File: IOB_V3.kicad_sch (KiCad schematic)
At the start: 7 parts, among them J1 Conn_01x02, J18 Conn_01x08, J2 Conn_01x03, U1 REF3033

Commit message: Layout WIP
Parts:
- J18: footprint Connector_IDC:IDC-Header_2x04_P2.54mm_Horizontal -> (none)
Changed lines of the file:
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@@
       (effects (font (size 1.27 1.27)) (justify left))
     )
-    (property "Footprint" "Connector_IDC:IDC-Header_2x04_P2.54mm_Horizontal" (id 2) (at 135.255 130.048 0)
+    (property "Footprint" "" (id 2) (at 135.255 130.048 0)
       (effects (font (size 1.27 1.27)) hide)
     )
@@
       (reference "#PWR0134") (unit 1) (value "GNDD") (footprint "")
     )
-    (path "/534d7b1f-d272-47da-b7a1-47aab2c48175/88cdcfe4-f642-4f46-a92c-2fc337766e9b"
+    (path "/534d7b1f-d272-47da-b7a1-47aab2c48175/1e98888a-427d-4a31-a7dd-97b8504ac365"
       (reference "#PWR0135") (unit 1) (value "GNDD") (footprint "")
     )
@@
     )
     (path "/534d7b1f-d272-47da-b7a1-47aab2c48175/5ea038cb-816d-4c36-bb7b-109706ba09b8"
-      (reference "D14") (unit 1) (value "LED") (footprint "LED_THT:LED_D1.8mm_W3.3mm_H2.4mm")
+      (reference "D14") (unit 1) (value "LED") (footprint "LED_SMD:LED_0603_1608Metric")
     )
     (path "/534d7b1f-d272-47da-b7a1-47aab2c48175/3aab0d4c-b03f-4a2b-bb8a-5ed68b4e7455"
-      (reference "D15") (unit 1) (value "LED") (footprint "LED_THT:LED_D1.8mm_W3.3mm_H2.4mm")
+      (reference "D15") (unit 1) (value "LED") (footprint "LED_SMD:LED_0603_1608Metric")
     )
     (path "/534d7b1f-d272-47da-b7a1-47aab2c48175/e259e01a-e686-48b7-b946-0f838b7ef786"
-      (reference "D16") (unit 1) (value "LED") (footprint "LED_THT:LED_D1.8mm_W3.3mm_H2.4mm")
+      (reference "D16") (unit 1) (value "LED") (footprint "LED_SMD:LED_0603_1608Metric")
     )
     (path "/534d7b1f-d272-47da-b7a1-47aab2c48175/08207f2a-291d-44df-8ce7-49d0dd8abd06"
-      (reference "D17") (unit 1) (value "LED") (footprint "LED_THT:LED_D1.8mm_W3.3mm_H2.4mm")
+      (reference "D17") (unit 1) (value "LED") (footprint "LED_SMD:LED_0603_1608Metric")
     )
     (path "/e7136250-cee6-4520-acb7-2950e0829e43/7426b94e-ffc2-452e-843f-c6ffae4705a2/52b8c382-e38e-4898-9fb4-9d3f624b54c7"
@@
     )
     (path "/e7a61089-3c45-4246-9e2f-067953569569"
-      (reference "J18") (unit 1) (value "Conn_01x08") (footprint "Connector_IDC:IDC-Header_2x04_P2.54mm_Horizontal")
+      (reference "J18") (unit 1) (value "Conn_01x08") (footprint "Connector_IDC:IDC-Header_2x04_P2.54mm_Vertical")
     )
     (path "/534d7b1f-d272-47da-b7a1-47aab2c48175/af1dd001-2f93-4b0a-9bcf-1f08059fc4a7"
@@
       (reference "SW2") (unit 1) (value "SW_Push_Dual") (footprint "TXV_Library_Footprints:SW_SPST_CK_RS282G05A3_and_THT")
     )
-    (path "/534d7b1f-d272-47da-b7a1-47aab2c48175/a325f198-534a-4f13-b7fd-b75bb8d3ea8f"
+    (path "/534d7b1f-d272-47da-b7a1-47aab2c48175/179c61ef-4bb1-49e7-a31d-9f9c899ae1c2"
       (reference "SW3") (unit 1) (value "SW_DIP_x08") (footprint "TXV_Library_Footprints:8_Pin_DIP_Switch")
     )

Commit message: Connectors change and part side flip
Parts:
- J18: footprint (none) -> Connector_IDC:IDC-Header_2x04_P2.54mm_Vertical
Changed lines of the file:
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@@
       (effects (font (size 1.27 1.27)) (justify left))
     )
-    (property "Footprint" "" (id 2) (at 135.255 130.048 0)
+    (property "Footprint" "Connector_IDC:IDC-Header_2x04_P2.54mm_Vertical" (id 2) (at 135.255 130.048 0)
       (effects (font (size 1.27 1.27)) hide)
     )
@@
       (reference "#PWR0137") (unit 1) (value "GNDD") (footprint "")
     )
-    (path "/534d7b1f-d272-47da-b7a1-47aab2c48175/86e1fb6b-02f5-44d9-be5a-dcc9d4ffc2e8"
+    (path "/534d7b1f-d272-47da-b7a1-47aab2c48175/31cd537c-8080-4893-996d-cf5dfc73426b"
       (reference "#PWR0138") (unit 1) (value "+5V") (footprint "")
     )
@@
       (reference "#PWR0139") (unit 1) (value "GNDD") (footprint "")
     )
-    (path "/534d7b1f-d272-47da-b7a1-47aab2c48175/573d7cc1-f5ea-48f8-9a0b-1e87d7df0d37"
-      (reference "#PWR0140") (unit 1) (value "GNDD") (footprint "")
+    (path "/534d7b1f-d272-47da-b7a1-47aab2c48175/b6659546-cd20-4177-96e0-bac10a28c326"
+      (reference "#PWR0140") (unit 1) (value "+5V") (footprint "")
     )
     (path "/534d7b1f-d272-47da-b7a1-47aab2c48175/d1457e9e-cd6f-4eac-a387-b31614edcffe"
       (reference "#PWR0141") (unit 1) (value "+3.3V") (footprint "")
     )
-    (path "/534d7b1f-d272-47da-b7a1-47aab2c48175/60eaa4dd-d726-4d7e-a298-4ff4d8f59925"
-      (reference "#PWR0142") (unit 1) (value "+5V") (footprint "")
+    (path "/534d7b1f-d272-47da-b7a1-47aab2c48175/7ebfcebf-b817-46ec-9695-1ccfc3c9960a"
+      (reference "#PWR0142") (unit 1) (value "GNDD") (footprint "")
     )
     (path "/534d7b1f-d272-47da-b7a1-47aab2c48175/221a7428-fe18-4c36-8179-294aaa90dd67"
       (reference "#PWR0143") (unit 1) (value "GNDA") (footprint "")
     )
-    (path "/534d7b1f-d272-47da-b7a1-47aab2c48175/fde89670-540f-4d7e-82e1-0078eae3cc64"
+    (path "/534d7b1f-d272-47da-b7a1-47aab2c48175/2a690fd6-2e13-4f52-bc32-d94631f9979b"
       (reference "#PWR0144") (unit 1) (value "GNDD") (footprint "")
     )
@@
       (reference "J16") (unit 1) (value "Conn_02x04_Odd_Even") (footprint "Connector_PinHeader_1.27mm:PinHeader_2x04_P1.27mm_Vertical_SMD")
     )
-    (path "/534d7b1f-d272-47da-b7a1-47aab2c48175/cd1d0e38-6320-4e6b-bf2a-3f5fcc7479ec"
-      (reference "J17") (unit 1) (value "Conn_01x04_MountingPin") (footprint "Connector_JST:JST_GH_BM04B-GHS-TBT_1x04-1MP_P1.25mm_Vertical")
+    (path "/534d7b1f-d272-47da-b7a1-47aab2c48175/ab44cab5-203b-4fac-b4ee-b824a1ef8e82"
+      (reference "J17") (unit 1) (value "TFC-103-01-F-D") (footprint "SAMTEC_TFC-103-01-F-D")
     )
     (path "/e7a61089-3c45-4246-9e2f-067953569569"
       (reference "J18") (unit 1) (value "Conn_01x08") (footprint "Connector_IDC:IDC-Header_2x04_P2.54mm_Vertical")
     )
-    (path "/534d7b1f-d272-47da-b7a1-47aab2c48175/af1dd001-2f93-4b0a-9bcf-1f08059fc4a7"
-      (reference "J19") (unit 1) (value "Conn_01x04_MountingPin") (footprint "Connector_JST:JST_GH_BM04B-GHS-TBT_1x04-1MP_P1.25mm_Vertical")
+    (path "/534d7b1f-d272-47da-b7a1-47aab2c48175/2208bac6-d2f1-4625-9045-1586d304572f"
+      (reference "J19") (unit 1) (value "TFC-103-01-F-D") (footprint "SAMTEC_TFC-103-01-F-D")
     )
     (path "/e7136250-cee6-4520-acb7-2950e0829e43/7426b94e-ffc2-452e-843f-c6ffae4705a2/6e5b9b26-db0d-4a77-8094-4bf066d10ecc"
@@
       (reference "TP2") (unit 1) (value "TestPoint") (footprint "TestPoint:TestPoint_THTPad_D1.0mm_Drill0.5mm")
     )
+    (path "/534d7b1f-d272-47da-b7a1-47aab2c48175/5b0d194e-8006-4f60-b614-a7daa5913b1a"
+      (reference "TP3") (unit 1) (value "TestPoint") (footprint "TestPoint:TestPoint_THTPad_D1.0mm_Drill0.5mm")
+    )
+    (path "/534d7b1f-d272-47da-b7a1-47aab2c48175/6c1daa0e-f97d-47ca-9763-5d736781736f"
+      (reference "TP4") (unit 1) (value "TestPoint") (footprint "TestPoint:TestPoint_THTPad_D1.0mm_Drill0.5mm")
+    )
+    (path "/534d7b1f-d272-47da-b7a1-47aab2c48175/e6bf6322-399b-44c9-a53a-e6d8c3dd4b6f"
+      (reference "TP5") (unit 1) (value "TestPoint") (footprint "TestPoint:TestPoint_THTPad_D1.0mm_Drill0.5mm")
+    )
+    (path "/534d7b1f-d272-47da-b7a1-47aab2c48175/2182db2c-e124-4535-890c-f41babccc9ab"
+      (reference "TP6") (unit 1) (value "TestPoint") (footprint "TestPoint:TestPoint_THTPad_D1.0mm_Drill0.5mm")
+    )
     (path "/31b062d9-fa48-4ba2-b857-360e76517386"

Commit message: Routing complete. Stitching missing
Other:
- sheet MCU ports: added En1, En10, En11, En12, En2, En3, En4, En5, En6, En7, En8, En9, OneWire; removed EXT_CLK, GPIO20, GPIO21, GPIO22, GPIO23, I2C1_SCL, PWM2, PWM3, PWM4, PWM6, PWM7, SPI1_MISO, SPI1_~{CS}
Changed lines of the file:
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@@
       (effects (font (size 1.27 1.27)) (justify left))
     )
-    (pin "PWM2" bidirectional (at 188.468 129.54 0)
-      (effects (font (size 1.27 1.27)) (justify right))
-    )
-    (pin "PWM3" bidirectional (at 188.468 132.08 0)
-      (effects (font (size 1.27 1.27)) (justify right))
-    )
-    (pin "PWM7" bidirectional (at 188.468 142.24 0)
-      (effects (font (size 1.27 1.27)) (justify right))
-    )
-    (pin "PWM6" bidirectional (at 188.468 139.7 0)
-      (effects (font (size 1.27 1.27)) (justify right))
-    )
-    (pin "PWM4" bidirectional (at 188.468 134.62 0)
-      (effects (font (size 1.27 1.27)) (justify right))
-    )
-    (pin "I2C1_SCL" output (at 188.468 69.977 0)
-      (effects (font (size 1.27 1.27)) (justify right))
-    )
-    (pin "SPI1_MISO" input (at 188.468 74.295 0)
-      (effects (font (size 1.27 1.27)) (justify right))
-    )
-    (pin "SPI1_~{CS}" output (at 188.468 76.835 0)
-      (effects (font (size 1.27 1.27)) (justify right))
-    )
-    (pin "EXT_CLK" output (at 188.468 72.263 0)
+    (pin "En9" bidirectional (at 188.468 129.54 0)
+      (effects (font (size 1.27 1.27)) (justify right))
+    )
+    (pin "En5" bidirectional (at 188.468 132.08 0)
+      (effects (font (size 1.27 1.27)) (justify right))
+    )
+    (pin "En12" bidirectional (at 188.468 142.24 0)
+      (effects (font (size 1.27 1.27)) (justify right))
+    )
+    (pin "En11" bidirectional (at 188.468 139.7 0)
+      (effects (font (size 1.27 1.27)) (justify right))
+    )
+    (pin "En10" bidirectional (at 188.468 134.62 0)
+      (effects (font (size 1.27 1.27)) (justify right))
+    )
+    (pin "En4" output (at 188.468 69.977 0)
+      (effects (font (size 1.27 1.27)) (justify right))
+    )
+    (pin "En7" input (at 188.468 74.295 0)
+      (effects (font (size 1.27 1.27)) (justify right))
+    )
+    (pin "En8" output (at 188.468 76.835 0)
+      (effects (font (size 1.27 1.27)) (justify right))
+    )
+    (pin "En3" output (at 188.468 72.263 0)
       (effects (font (size 1.27 1.27)) (justify right))
     )
@@
       (effects (font (size 1.27 1.27)) (justify right))
     )
-    (pin "GPIO23" bidirectional (at 188.468 127.127 0)
-      (effects (font (size 1.27 1.27)) (justify right))
-    )
-    (pin "GPIO21" bidirectional (at 188.468 122.047 0)
-      (effects (font (size 1.27 1.27)) (justify right))
-    )
-    (pin "GPIO22" bidirectional (at 188.468 124.587 0)
-      (effects (font (size 1.27 1.27)) (justify right))
-    )
-    (pin "GPIO20" bidirectional (at 188.468 119.507 0)
+    (pin "En2" bidirectional (at 188.468 127.127 0)
+      (effects (font (size 1.27 1.27)) (justify right))
+    )
+    (pin "En6" bidirectional (at 188.468 122.047 0)
+      (effects (font (size 1.27 1.27)) (justify right))
+    )
+    (pin "En1" bidirectional (at 188.468 124.587 0)
+      (effects (font (size 1.27 1.27)) (justify right))
+    )
+    (pin "OneWire" bidirectional (at 188.468 119.507 0)
       (effects (font (size 1.27 1.27)) (justify right))
     )
@@
       (reference "TP4") (unit 1) (value "TestPoint") (footprint "TestPoint:TestPoint_THTPad_D1.0mm_Drill0.5mm")
     )
-    (path "/534d7b1f-d272-47da-b7a1-47aab2c48175/bf8e7d38-040e-462b-bcfc-7258ba8c1b2e"
+    (path "/534d7b1f-d272-47da-b7a1-47aab2c48175/33b0de3b-c41b-4e4a-865c-fa50373d2952"
       (reference "TP5") (unit 1) (value "TestPoint") (footprint "TestPoint:TestPoint_THTPad_D1.0mm_Drill0.5mm")
     )

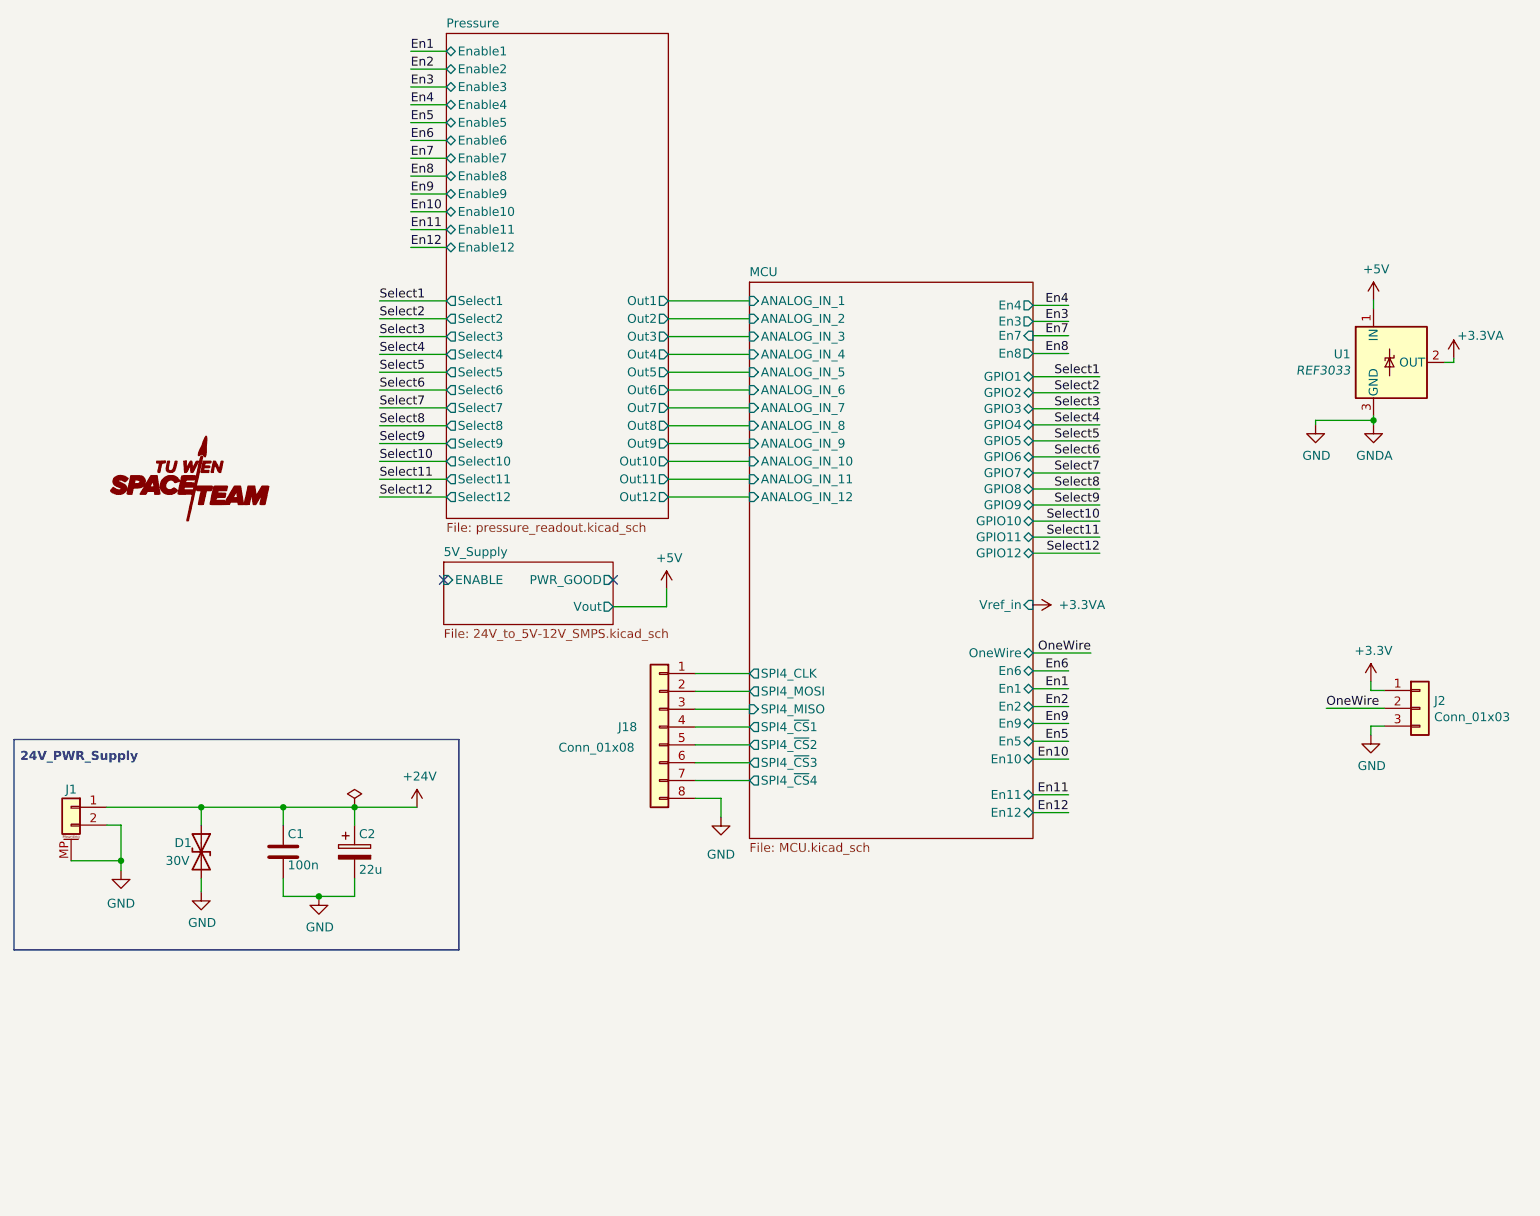
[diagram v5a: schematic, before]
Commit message: Added 2nd SPI4 connector
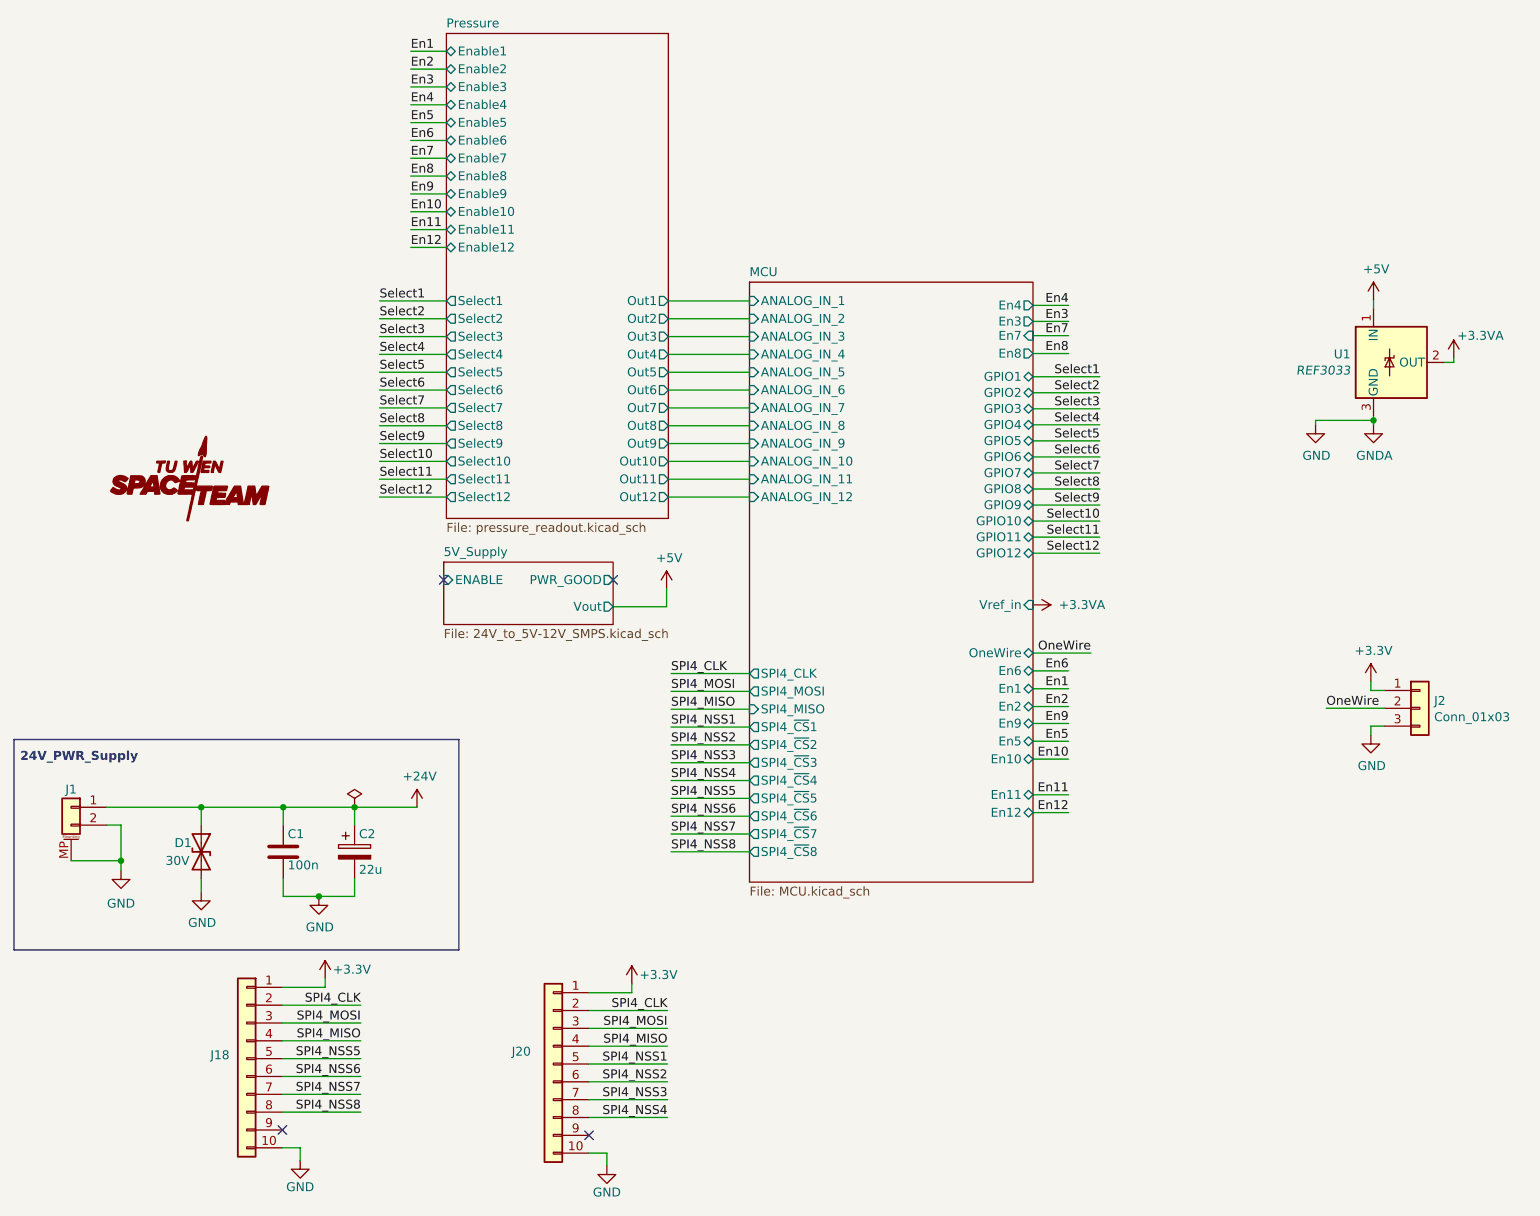
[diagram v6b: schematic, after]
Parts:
- removed J18: Conn_01x08, Connector_IDC:IDC-Header_2x04_P2.54mm_Vertical, symbol Connector_Generic:Conn_01x08
- added J18, J20: (no value), symbol Connector_Generic:Conn_01x10
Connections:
- net +3V3: now also J18.1 (Pin_1), J20.1 (Pin_1)
- net GND: now also J18.10 (Pin_10), J20.10 (Pin_10)
- new net SPI4_CLK: J18.2 (Pin_2), J20.2 (Pin_2)
- new net SPI4_MISO: J18.4 (Pin_4), J20.4 (Pin_4)
- new net SPI4_MOSI: J18.3 (Pin_3), J20.3 (Pin_3)
- new net SPI4_NSS1: J20.5 (Pin_5)
- new net SPI4_NSS2: J20.6 (Pin_6)
- new net SPI4_NSS3: J20.7 (Pin_7)
- new net SPI4_NSS4: J20.8 (Pin_8)
- new net SPI4_NSS5: J18.5 (Pin_5)
- new net SPI4_NSS6: J18.6 (Pin_6)
- new net SPI4_NSS7: J18.7 (Pin_7)
- new net SPI4_NSS8: J18.8 (Pin_8)
- no-connect marks 2 -> 4
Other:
- sheet MCU ports: added SPI4_~{CS}5, SPI4_~{CS}6, SPI4_~{CS}7, SPI4_~{CS}8; removed none
